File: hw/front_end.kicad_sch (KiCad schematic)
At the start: 6 parts, among them Q4 SSM6P35AFE, Q5 SSM6P35AFE

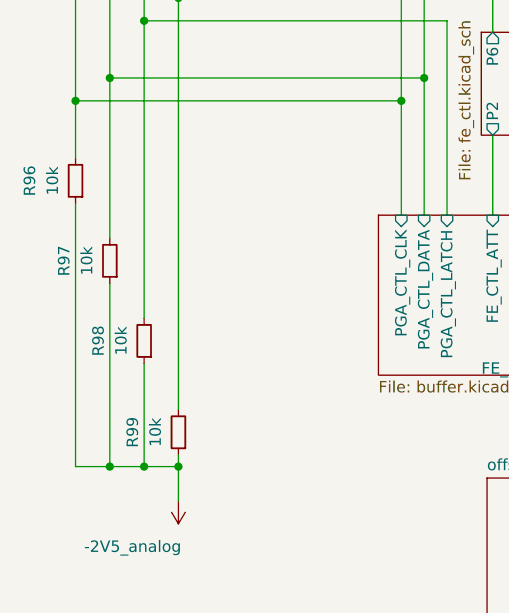
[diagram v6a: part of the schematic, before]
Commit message: Reduced PGA level translator resistors from 10k to 5k1
Had erroneously loaded 18k and these didn't work. Even though
the signals looked OK the gain word was not picked up by the
device w/o errors. Maybe the fall times were slow and had
noise components that caused spurious clock edges?

In any case: with 5k1 it now works...
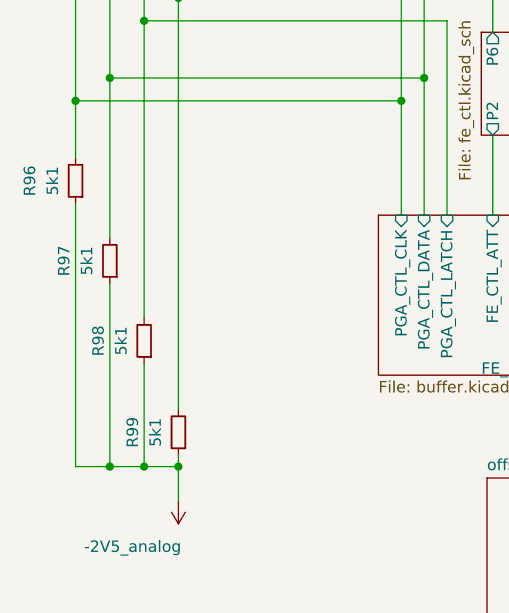
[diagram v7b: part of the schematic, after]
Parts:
- R96, R97, R98, R99: value 10k -> 5k1
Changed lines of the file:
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@@
       (effects (font (size 1.27 1.27)))
     )
-    (property "Value" "10k" (at 68.58 146.05 90)
+    (property "Value" "5k1" (at 68.58 146.05 90)
       (effects (font (size 1.27 1.27)))
     )
@@
       (effects (font (size 1.27 1.27)))
     )
-    (property "Value" "10k" (at 57.15 118.11 90)
+    (property "Value" "5k1" (at 57.15 118.11 90)
       (effects (font (size 1.27 1.27)))
     )
@@
       (effects (font (size 1.27 1.27)))
     )
-    (property "Value" "10k" (at 64.77 135.89 90)
+    (property "Value" "5k1" (at 64.77 135.89 90)
       (effects (font (size 1.27 1.27)))
     )
@@
       (effects (font (size 1.27 1.27)))
     )
-    (property "Value" "10k" (at 60.96 127 90)
-      (effects (font (size 1.27 1.27)))
-    )
+    (property "Value" "5k1" (at 60.96 127 90)
+      (effects (font (size 1.27 1.27)))
+    )

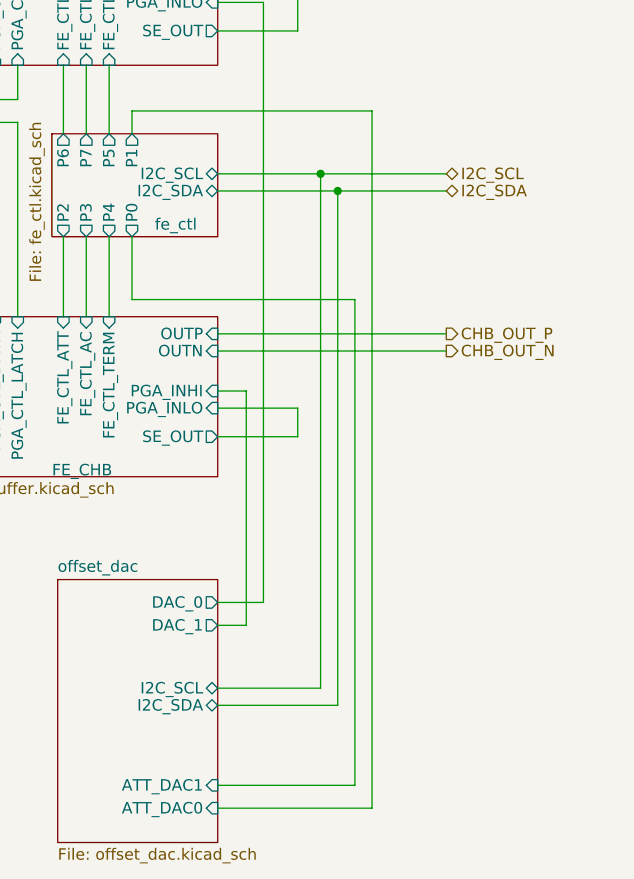
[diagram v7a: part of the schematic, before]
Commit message: Connected FEC i2c to 3V3
This permits omitting the i2c level converted if the DAC is not used.
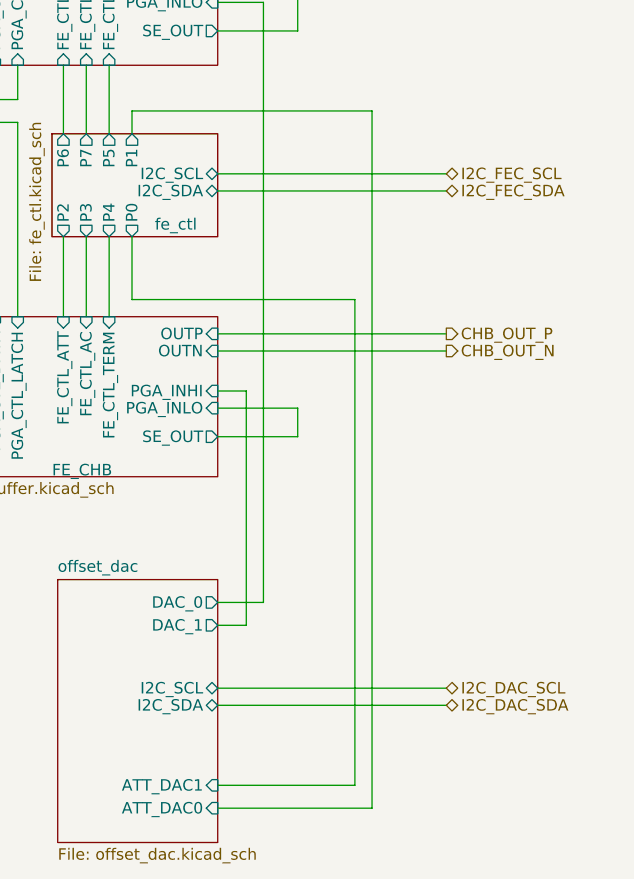
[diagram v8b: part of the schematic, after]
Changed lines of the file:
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@@
   (junction (at 59.69 109.22) (diameter 0) (color 0 0 0 0)
   )
-  (junction (at 136.525 107.95) (diameter 0) (color 0 0 0 0)
-  )
   (junction (at 71.12 97.79) (diameter 0) (color 0 0 0 0)
   )
@@
   (junction (at 77.47 38.1) (diameter 0) (color 0 0 0 0)
   )
-  (junction (at 134.62 106.045) (diameter 0) (color 0 0 0 0)
-  )
   (junction (at 71.12 149.86) (diameter 0) (color 0 0 0 0)
   )
@@
   (junction (at 67.31 149.86) (diameter 0) (color 0 0 0 0)
   )
-  (wire (pts (xy 123.19 106.045) (xy 134.62 106.045))
+  (wire (pts (xy 123.19 106.045) (xy 148.59 106.045))
     (stroke (width 0) (type default))
   )
@@
     (stroke (width 0) (type default))
   )
-  (wire (pts (xy 136.525 165.1) (xy 136.525 107.95))
-    (stroke (width 0) (type default))
-  )
   (wire (pts (xy 67.31 100.33) (xy 67.31 133.35))
     (stroke (width 0) (type default))
@@
     (stroke (width 0) (type default))
   )
-  (wire (pts (xy 134.62 106.045) (xy 148.59 106.045))
-    (stroke (width 0) (type default))
-  )
   (wire (pts (xy 59.69 57.15) (xy 59.69 38.1))
     (stroke (width 0) (type default))
@@
     (stroke (width 0) (type default))
   )
-  (wire (pts (xy 123.19 165.1) (xy 136.525 165.1))
+  (wire (pts (xy 123.19 165.1) (xy 148.59 165.1))
     (stroke (width 0) (type default))
   )
@@
     (stroke (width 0) (type default))
   )
+  (wire (pts (xy 123.19 163.195) (xy 148.59 163.195))
+    (stroke (width 0) (type default))
+  )
   (wire (pts (xy 113.665 120.015) (xy 138.43 120.015))
     (stroke (width 0) (type default))
@@
     (stroke (width 0) (type default))
   )
-  (wire (pts (xy 136.525 107.95) (xy 123.19 107.95))
+  (wire (pts (xy 123.19 107.95) (xy 148.59 107.95))
     (stroke (width 0) (type default))
   )
@@
     (stroke (width 0) (type default))
   )
-  (wire (pts (xy 148.59 107.95) (xy 136.525 107.95))
-    (stroke (width 0) (type default))
-  )
-  (wire (pts (xy 123.19 163.195) (xy 134.62 163.195))
-    (stroke (width 0) (type default))
-  )
   (wire (pts (xy 111.125 113.03) (xy 111.125 121.92))
     (stroke (width 0) (type default))
@@
     (stroke (width 0) (type default))
   )
-  (wire (pts (xy 134.62 163.195) (xy 134.62 106.045))
-    (stroke (width 0) (type default))
-  )
   (wire (pts (xy 71.12 73.66) (xy 71.12 97.79))
     (stroke (width 0) (type default))
@@
     (stroke (width 0) (type default))
   )
-  (hierarchical_label "I2C_SDA" (shape bidirectional) (at 148.59 107.95 0) (fields_autoplaced)
+  (hierarchical_label "I2C_FEC_SDA" (shape bidirectional) (at 148.59 107.95 0) (fields_autoplaced)
+    (effects (font (size 1.27 1.27)) (justify left))
+  )
+  (hierarchical_label "I2C_DAC_SCL" (shape bidirectional) (at 148.59 163.195 0) (fields_autoplaced)
     (effects (font (size 1.27 1.27)) (justify left))
   )
@@
     (effects (font (size 1.27 1.27)) (justify left))
   )
-  (hierarchical_label "I2C_SCL" (shape bidirectional) (at 148.59 106.045 0) (fields_autoplaced)
+  (hierarchical_label "I2C_FEC_SCL" (shape bidirectional) (at 148.59 106.045 0) (fields_autoplaced)
     (effects (font (size 1.27 1.27)) (justify left))
   )
@@
     (effects (font (size 1.27 1.27)) (justify left))
   )
+  (hierarchical_label "I2C_DAC_SDA" (shape bidirectional) (at 148.59 165.1 0) (fields_autoplaced)
+    (effects (font (size 1.27 1.27)) (justify left))
+  )
